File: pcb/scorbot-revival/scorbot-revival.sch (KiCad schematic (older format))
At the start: 3 parts, among them J1 DB-50, J2 Raspberry_Pi_2_3, U1 L293D

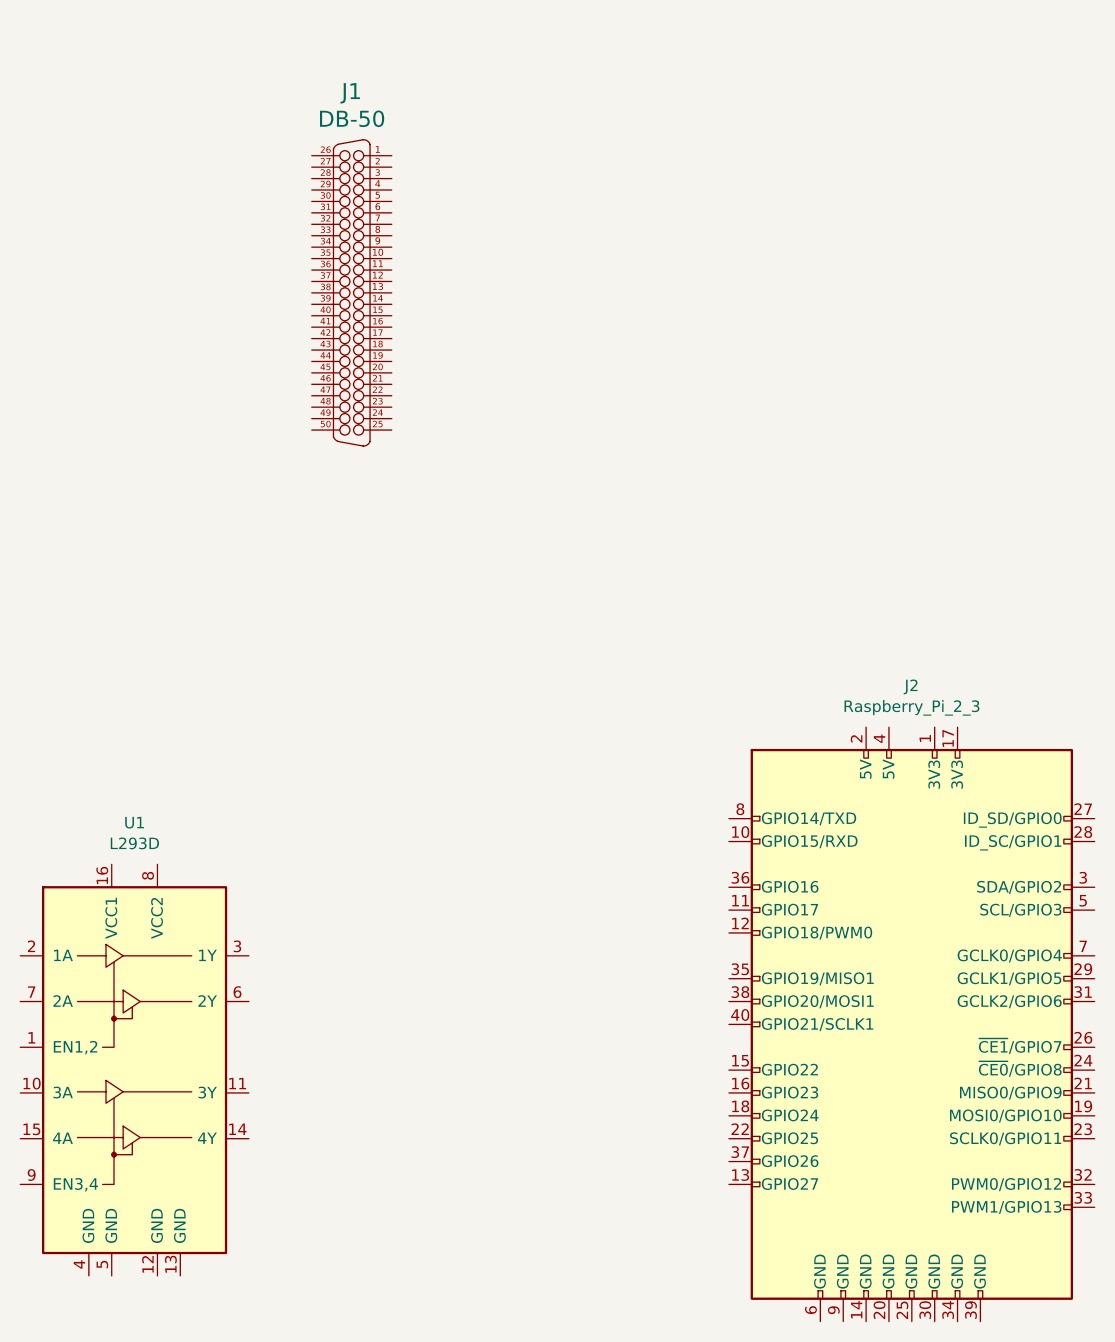
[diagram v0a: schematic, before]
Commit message: [pcb] added labels to DB50 connector in schematic
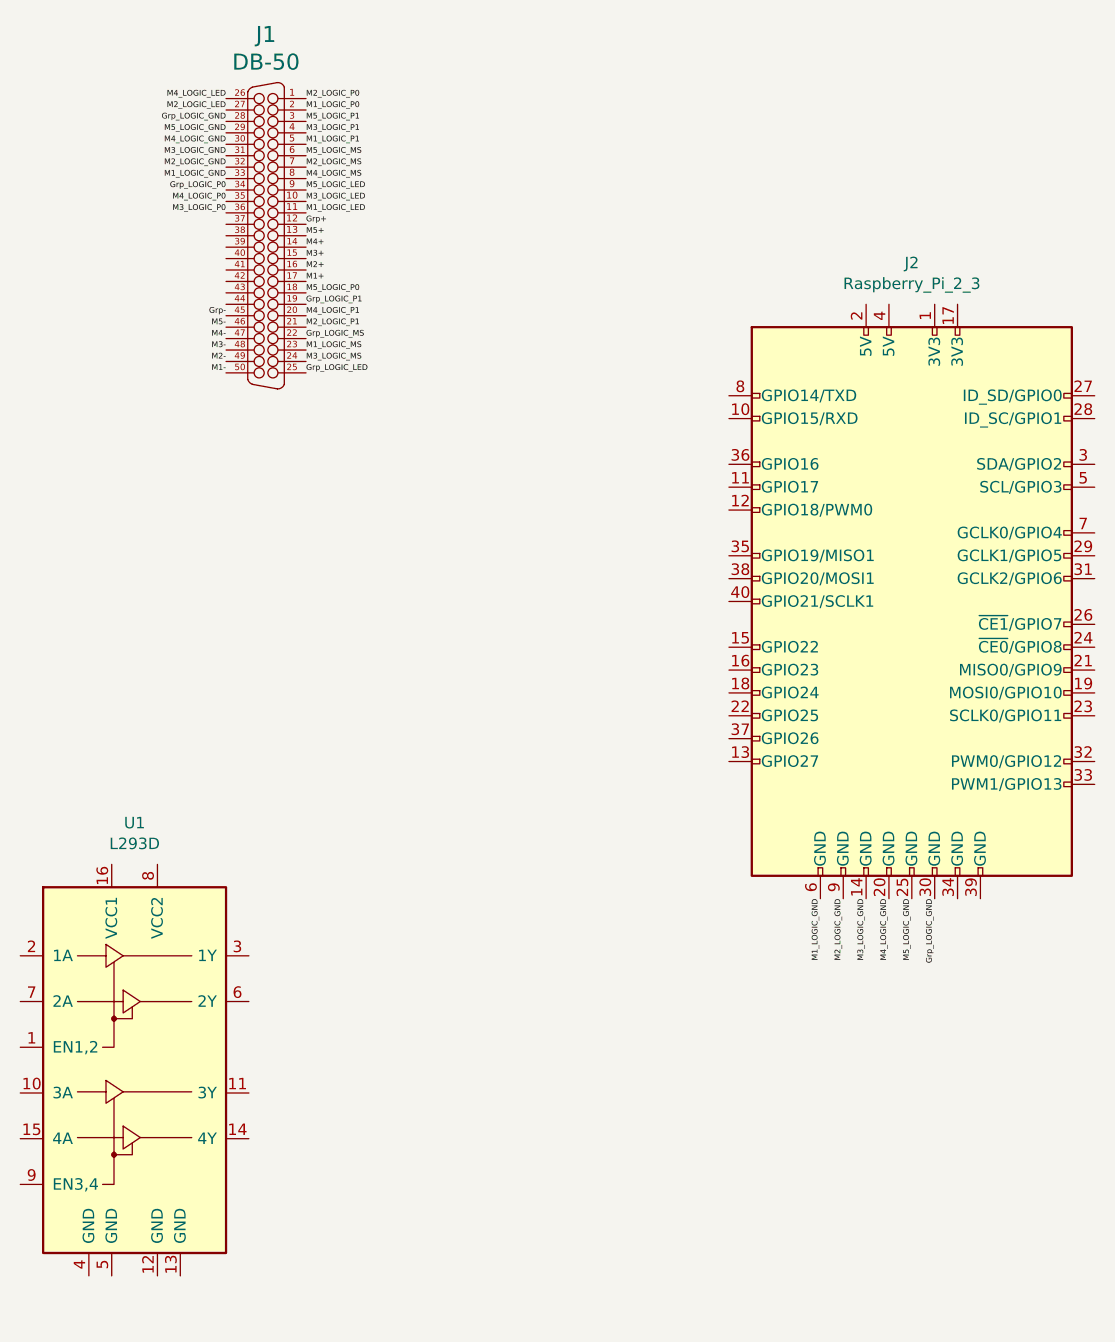
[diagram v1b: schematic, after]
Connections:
- net M2_LOGIC_P0: now reaches J1.1
- net M3_LOGIC_LED: now reaches J1.10
- net M1_LOGIC_LED: now reaches J1.11
- net Grp+: now reaches J1.12
- net M5+: now reaches J1.13
- net M4+: now reaches J1.14
- net M3+: now reaches J1.15
- net M2+: now reaches J1.16
- net M1+: now reaches J1.17
- net M5_LOGIC_P0: now reaches J1.18
- net Grp_LOGIC_P1: now reaches J1.19
- net M1_LOGIC_P0: now reaches J1.2
- net M4_LOGIC_P1: now reaches J1.20
- net M2_LOGIC_P1: now reaches J1.21
- net Grp_LOGIC_MS: now reaches J1.22
- net M1_LOGIC_MS: now reaches J1.23
- net M3_LOGIC_MS: now reaches J1.24
- net Grp_LOGIC_LED: now reaches J1.25
- net M4_LOGIC_LED: now reaches J1.26
- net M2_LOGIC_LED: now reaches J1.27
- net Grp_LOGIC_GND: now reaches J1.28
- net Grp_LOGIC_GND: now also J2.30 (GND)
- net M5_LOGIC_GND: now reaches J1.29
- net M5_LOGIC_GND: now also J2.25 (GND)
- net M5_LOGIC_P1: now reaches J1.3
- net M4_LOGIC_GND: now reaches J1.30
- net M4_LOGIC_GND: now also J2.20 (GND)
- net M3_LOGIC_GND: now reaches J1.31
- net M3_LOGIC_GND: now also J2.14 (GND)
- net M2_LOGIC_GND: now reaches J1.32
- net M2_LOGIC_GND: now also J2.9 (GND)
- net M1_LOGIC_GND: now reaches J1.33
- net M1_LOGIC_GND: now also J2.6 (GND)
- net Grp_LOGIC_P0: now reaches J1.34
- net M4_LOGIC_P0: now reaches J1.35
- net M3_LOGIC_P0: now reaches J1.36
- net M3_LOGIC_P1: now reaches J1.4
- net Grp-: now reaches J1.45
- net M5-: now reaches J1.46
- net M4-: now reaches J1.47
- net M3-: now reaches J1.48
- net M2-: now reaches J1.49
- net M1_LOGIC_P1: now reaches J1.5
- net M1-: now reaches J1.50
- net M5_LOGIC_MS: now reaches J1.6
- net M2_LOGIC_MS: now reaches J1.7
- net M4_LOGIC_MS: now reaches J1.8
- net M5_LOGIC_LED: now reaches J1.9
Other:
- moved on the sheet: J1, J2
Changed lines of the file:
@@
 L smisioto_connectors:DB-50 J1
 U 1 1 5DE13F75
-P 3400 2350
-F 0 "J1" H 3400 3230 70  0000 C CNN
-F 1 "DB-50" H 3400 3109 70  0000 C CNN
-F 2 "LibraryLoader:09665526612" H 3400 2350 60  0001 C CNN
-F 3 "" H 3400 2350 60  0000 C CNN
-	1    3400 2350
+P 3025 2100
+F 0 "J1" H 3025 2980 70  0000 C CNN
+F 1 "DB-50" H 3025 2859 70  0000 C CNN
+F 2 "LibraryLoader:09665526612" H 3025 2100 60  0001 C CNN
+F 3 "" H 3025 2100 60  0000 C CNN
+	1    3025 2100
 	1    0    0    -1
 $EndComp
@@
 L Connector:Raspberry_Pi_2_3 J2
 U 1 1 5DE8F286
-P 5850 5550
-F 0 "J2" H 5850 7031 50  0000 C CNN
-F 1 "Raspberry_Pi_2_3" H 5850 6940 50  0000 C CNN
-F 2 "Connector_PinHeader_2.54mm:PinHeader_2x20_P2.54mm_Vertical" H 5850 5550 50  0001 C CNN
-F 3 "https://www.raspberrypi.org/documentation/hardware/raspberrypi/schematics/rpi_SCH_3bplus_1p0_reduced.pdf" H 5850 5550 50  0001 C CNN
-	1    5850 5550
+P 5850 3700
+F 0 "J2" H 5850 5181 50  0000 C CNN
+F 1 "Raspberry_Pi_2_3" H 5850 5090 50  0000 C CNN
+F 2 "Connector_PinHeader_2.54mm:PinHeader_2x20_P2.54mm_Vertical" H 5850 3700 50  0001 C CNN
+F 3 "https://www.raspberrypi.org/documentation/hardware/raspberrypi/schematics/rpi_SCH_3bplus_1p0_reduced.pdf" H 5850 3700 50  0001 C CNN
+	1    5850 3700
 	1    0    0    -1
 $EndComp
+Text Label 2850 2700 2    25   ~ 0
+M1-
+Text Label 2850 2650 2    25   ~ 0
+M2-
+Text Label 2850 2600 2    25   ~ 0
+M3-
+Text Label 2850 2550 2    25   ~ 0
+M4-
+Text Label 2850 2500 2    25   ~ 0
+M5-
+Text Label 2850 2450 2    25   ~ 0
+Grp-
+Text Label 3200 2300 0    25   ~ 0
+M1+
+Text Label 3200 2250 0    25   ~ 0
+M2+
+Text Label 3200 2200 0    25   ~ 0
+M3+
+Text Label 3200 2150 0    25   ~ 0
+M4+
+Text Label 3200 2100 0    25   ~ 0
+M5+
+Text Label 3200 2050 0    25   ~ 0
+Grp+
+Text Label 2850 1850 2    25   ~ 0
+M1_LOGIC_GND
+Text Label 2850 1800 2    25   ~ 0
+M2_LOGIC_GND
+Text Label 2850 1750 2    25   ~ 0
+M3_LOGIC_GND
+Text Label 2850 1700 2    25   ~ 0
+M4_LOGIC_GND
+Text Label 2850 1650 2    25   ~ 0
+M5_LOGIC_GND
+Text Label 2850 1600 2    25   ~ 0
+Grp_LOGIC_GND
+Text Label 3200 2000 0    25   ~ 0
+M1_LOGIC_LED
+Text Label 2850 1550 2    25   ~ 0
+M2_LOGIC_LED
+Text Label 3200 1950 0    25   ~ 0
+M3_LOGIC_LED
+Text Label 2850 1500 2    25   ~ 0
+M4_LOGIC_LED
+Text Label 3200 1900 0    25   ~ 0
+M5_LOGIC_LED
+Text Label 3200 2700 0    25   ~ 0
+Grp_LOGIC_LED
+Text Label 3200 1700 0    25   ~ 0
+M1_LOGIC_P1
+Text Label 3200 2500 0    25   ~ 0
+M2_LOGIC_P1
+Text Label 3200 1650 0    25   ~ 0
+M3_LOGIC_P1
+Text Label 3200 2450 0    25   ~ 0
+M4_LOGIC_P1
+Text Label 3200 1600 0    25   ~ 0
+M5_LOGIC_P1
+Text Label 3200 2400 0    25   ~ 0
+Grp_LOGIC_P1
+Text Label 3200 1550 0    25   ~ 0
+M1_LOGIC_P0
+Text Label 3200 1500 0    25   ~ 0
+M2_LOGIC_P0
+Text Label 2850 2000 2    25   ~ 0
+M3_LOGIC_P0
+Text Label 2850 1950 2    25   ~ 0
+M4_LOGIC_P0
+Text Label 3200 2350 0    25   ~ 0
+M5_LOGIC_P0
+Text Label 2850 1900 2    25   ~ 0
+Grp_LOGIC_P0
+Text Label 3200 2600 0    25   ~ 0
+M1_LOGIC_MS
+Text Label 3200 1800 0    25   ~ 0
+M2_LOGIC_MS
+Text Label 3200 2650 0    25   ~ 0
+M3_LOGIC_MS
+Text Label 3200 1850 0    25   ~ 0
+M4_LOGIC_MS
+Text Label 3200 1750 0    25   ~ 0
+M5_LOGIC_MS
+Text Label 3200 2550 0    25   ~ 0
+Grp_LOGIC_MS
+Text Label 5450 5000 3    25   ~ 0
+M1_LOGIC_GND
+Text Label 5550 5000 3    25   ~ 0
+M2_LOGIC_GND
+Text Label 5650 5000 3    25   ~ 0
+M3_LOGIC_GND
+Text Label 5750 5000 3    25   ~ 0
+M4_LOGIC_GND
+Text Label 5850 5000 3    25   ~ 0
+M5_LOGIC_GND
+Text Label 5950 5000 3    25   ~ 0
+Grp_LOGIC_GND
 $EndSCHEMATC

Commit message: [pcb] add PIC16CE625-04I to schematic + pcbnew
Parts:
- added U2: PIC16CE625-04I_P, PIC16CE625-04I/P:PIC16CE625-04I&slash_P, symbol PIC16CE625-04I/P:PIC16CE625-04I_P
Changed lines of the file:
@@
 Text Label 5950 5000 3    25   ~ 0
 Grp_LOGIC_GND
+$Comp
+L PIC16CE625-04I/P:PIC16CE625-04I_P U2
+U 1 1 5DFA9FB6
+P 7600 3400
+F 0 "U2" H 9100 3787 60  0000 C CNN
+F 1 "PIC16CE625-04I_P" H 9100 3681 60  0000 C CNN
+F 2 "PIC16CE625-04I/P:PIC16CE625-04I&slash_P" H 9100 3640 60  0001 C CNN
+F 3 "" H 7600 3400 60  0000 C CNN
+	1    7600 3400
+	1    0    0    -1
+$EndComp
 $EndSCHEMATC

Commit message: [pcb] replace old PIC with PIC18F2431-E_SP
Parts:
- removed U2: PIC16CE625-04I_P, PIC16CE625-04I/P:PIC16CE625-04I&slash_P, symbol PIC16CE625-04I/P:PIC16CE625-04I_P
- added U2: PIC18F2431-E_SP, Package_DIP:DIP-28_W7.62mm, symbol PIC18F2431-E_SP:PIC18F2431-E_SP
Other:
- moved on the sheet: J2
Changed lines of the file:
@@
-	1    0    0    -1
-$EndComp
-$Comp
-L Connector:Raspberry_Pi_2_3 J2
-U 1 1 5DE8F286
-P 5850 3700
-F 0 "J2" H 5850 5181 50  0000 C CNN
-F 1 "Raspberry_Pi_2_3" H 5850 5090 50  0000 C CNN
-F 2 "Connector_PinHeader_2.54mm:PinHeader_2x20_P2.54mm_Vertical" H 5850 3700 50  0001 C CNN
-F 3 "https://www.raspberrypi.org/documentation/hardware/raspberrypi/schematics/rpi_SCH_3bplus_1p0_reduced.pdf" H 5850 3700 50  0001 C CNN
-	1    5850 3700
 	1    0    0    -1
 $EndComp
@@
 Text Label 3200 2550 0    25   ~ 0
 Grp_LOGIC_MS
-Text Label 5450 5000 3    25   ~ 0
+Text Label 4850 7250 3    25   ~ 0
 M1_LOGIC_GND
-Text Label 5550 5000 3    25   ~ 0
+Text Label 4950 7250 3    25   ~ 0
 M2_LOGIC_GND
-Text Label 5650 5000 3    25   ~ 0
+Text Label 5050 7250 3    25   ~ 0
 M3_LOGIC_GND
-Text Label 5750 5000 3    25   ~ 0
+Text Label 5150 7250 3    25   ~ 0
 M4_LOGIC_GND
-Text Label 5850 5000 3    25   ~ 0
+Text Label 5250 7250 3    25   ~ 0
 M5_LOGIC_GND
-Text Label 5950 5000 3    25   ~ 0
+Text Label 5350 7250 3    25   ~ 0
 Grp_LOGIC_GND
 $Comp
-L PIC16CE625-04I/P:PIC16CE625-04I_P U2
-U 1 1 5DFA9FB6
-P 7600 3400
-F 0 "U2" H 9100 3787 60  0000 C CNN
-F 1 "PIC16CE625-04I_P" H 9100 3681 60  0000 C CNN
-F 2 "PIC16CE625-04I/P:PIC16CE625-04I&slash_P" H 9100 3640 60  0001 C CNN
-F 3 "" H 7600 3400 60  0000 C CNN
-	1    7600 3400
+L PIC18F2431-E_SP:PIC18F2431-E_SP U2
+U 1 1 5E01D5FD
+P 8200 2250
+F 0 "U2" H 8200 3620 50  0000 C CNN
+F 1 "PIC18F2431-E_SP" H 8200 3529 50  0000 C CNN
+F 2 "Package_DIP:DIP-28_W7.62mm" H 8200 2250 50  0001 L BNN
+F 3 "PIC18F2431-E/SP-ND" H 8200 2250 50  0001 L BNN
+F 4 "SPDIP-28 Microchip" H 8200 2250 50  0001 L BNN "Field4"
+F 5 "PIC18F2431-E/SP" H 8200 2250 50  0001 L BNN "Field5"
+F 6 "https://www.digikey.com/product-detail/en/microchip-technology/PIC18F2431-E-SP/PIC18F2431-E-SP-ND/613546?utm_source=snapeda&utm_medium=aggregator&utm_campaign=symbol" H 8200 2250 50  0001 L BNN "Field6"
+F 7 "Microchip" H 8200 2250 50  0001 L BNN "Field7"
+F 8 "MCU 8-bit PIC18 PIC RISC 16KB Flash 5V 28-Pin SPDIP Tube" H 8200 2250 50  0001 L BNN "Field8"
+	1    8200 2250
 	1    0    0    -1
 $EndComp
+$Comp
+L Connector:Raspberry_Pi_2_3 J2
+U 1 1 5DE8F286
+P 5250 5950
+F 0 "J2" H 5250 7431 50  0000 C CNN
+F 1 "Raspberry_Pi_2_3" H 5250 7340 50  0000 C CNN
+F 2 "Connector_PinHeader_2.54mm:PinHeader_2x20_P2.54mm_Vertical" H 5250 5950 50  0001 C CNN
+F 3 "https://www.raspberrypi.org/documentation/hardware/raspberrypi/schematics/rpi_SCH_3bplus_1p0_reduced.pdf" H 5250 5950 50  0001 C CNN
+	1    5250 5950
+	1    0    0    -1
+$EndComp
